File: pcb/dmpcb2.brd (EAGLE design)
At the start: 100 x 100 mm, 65 parts, among them IC1 7805DT, IC2 L293D, IC4 LM358D, IC5 LM358D, J7 SJ-3523-SMT-TR, Q1 IRF530, Q2 IRF530

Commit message: borading2..
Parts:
- added DCMOTOR1: (no value), SparkFun-Connectors:1X02_2.54_SCREWTERM
- added JP1: (no value), jumper:JP2
- added X2: (no value), con-wago-500:W237-4
- added X3: (no value), con-wago-500:W237-102
- moved IC4 247.8 mm to (16.5, 56.5), turned to 90 degrees
- moved R15 180.1 mm to (6.35, 64.1)
- moved R16 177.9 mm to (-17.8, 58.4)
- moved R10 175.2 mm to (-12.7, 47.6)
- moved JP6 163.5 mm to (19.7, 38.1)
- moved JP5 160.4 mm to (19.7, 41.3)
- moved R11 158.7 mm to (-32.4, 62.2)
- moved JP4 149.4 mm to (19.7, 44.5), turned to 180 degrees
- moved R9 145.1 mm to (-5.71, 52.1)
- moved J8 142.9 mm to (20.3, 62.2)
- moved R12 125.8 mm to (41.3, 13.3), turned to 270 degrees
- moved R13 112.5 mm to (59.7, 14.0), turned to 270 degrees
- moved JP3 110.0 mm to (8.26, 48.9)
- moved C7 48.2 mm to (13.3, 7.62), turned to 270 degrees
- moved U$2 10.8 mm to (19.7, 24.8)
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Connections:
- new net N$11: DCMOTOR1.P1, IC2.14
- new net N$12: DCMOTOR1.P2, IC2.11
- net +5V: now also JP1.3
- net A1: now also X2.2
- net A2: now also X2.1
- net B1: now also X2.3
- net B2: now also X2.4
- net GND: now also X3.2
- net V+: now also JP1.1
- net VMOT: now also JP1.2, X3.1
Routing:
- net +5V: track 184.9 -> 350.7 mm, vias 1 -> 2
- net V+: track 89.4 -> 211.0 mm
- net DRV8825SLP: track 0.00 -> 88.9 mm
- net DRV8825STEP: track 0.00 -> 81.5 mm
- net DRV8825DIR: track 0.00 -> 76.6 mm
- net N$57: track 0.00 -> 32.3 mm
- net N$11: track 0.00 -> 25.4 mm
- net N$58: track 0.00 -> 23.3 mm
- net N$59: track 0.00 -> 22.3 mm
- net N$12: track 0.00 -> 21.9 mm
- net VMOT: track 0.00 -> 19.1 mm
- net N$5: track 0.00 -> 13.6 mm
- net B2: track 0.00 -> 9.88 mm
- net A2: track 0.00 -> 9.88 mm
- net A1: track 0.00 -> 8.80 mm
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
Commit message: routing done
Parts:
- removed DCMOTOR, DCMOTOR1, SENSOR, SWITCHLOAD, SWITCHLOAD1: (no value), SparkFun-Connectors:1X02_2.54_SCREWTERM
- removed JP8: (no value), jumper:JP1
- removed SV2: (no value), con-lstb:MA08-1
- added 14/DAC: (no value), jumper:JP1
- added J3: (no value), SparkFun-Connectors:1X08
- added J4: (no value), SparkFun-Connectors:1X03_LOCK_LONGPADS
- added X4, X5, X6, X7, X8: (no value), con-wago-500:W237-102
- moved R11 47.7 mm to (15.2, 59.7)
- moved R16 40.0 mm to (21.6, 65.4), turned to 90 degrees
- moved R10 28.8 mm to (15.2, 54.6)
- moved R9 21.6 mm to (15.2, 57.1)
- moved JP3 15.7 mm to (21.6, 57.1), turned to 270 degrees
- moved X1 10.9 mm to (93.3, 85.7), flipped to the bottom, turned to 270 degrees
- moved C3 10.9 mm to (95.2, 74.9), turned to 180 degrees
- moved JP6 9.88 mm to (12.7, 45.1), turned to 90 degrees
- moved R13 9.67 mm to (63.5, 5.08)
- moved R12 9.38 mm to (36.8, 5.08)
- moved IC4 7.73 mm to (15.2, 64.1)
- moved J8 7.62 mm to (20.3, 69.8)
- moved 3.3V 7.62 mm to (82.5, 66.0)
- moved 5V 7.62 mm to (88.3, 66.0)
- moved GND 7.62 mm to (94.0, 66.0)
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- renumbered JP7 to EXT_5V
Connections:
- removed net LM293EN: IC2.1, SV2.3
- removed net LM293IN01: IC2.2, SV2.4
- removed net LM293IN02: IC2.7, SV2.5
- new net H-BRDIGE_A_02: IC2.7, J3.5
- new net H-BRIDGE_A_01: IC2.2, J3.4
- new net H-BRIDGE_A_EN: IC2.1, J3.3
- new net H-BRIDGE_B_01: IC2.15, J4.3
- new net H-BRIDGE_B_02: IC2.10, J4.2
- new net H-BRIDGE_B_EN: IC2.9, J4.1
- net +5V: now also X8.1; no longer SENSOR.P2
- net BETTERAUDIOOUT: now also 14/DAC.2; no longer JP8.2
- net BUTTON01: now also J3.1; no longer SV2.1
- net BUTTON02: now also J3.2; no longer SV2.2
- net DRV8825DIR: now also J1.1; no longer J1.2
- net DRV8825EN: now also J1.5; no longer J1.1
- net DRV8825SLP: now also J1.3; no longer J1.5
- net DRV8825STEP: now also J1.2; no longer J1.3
- net M1: now also X4.2; no longer SWITCHLOAD.P1
- net M2: now also X5.2; no longer SWITCHLOAD1.P1
- net MAX7219CLK: now also J3.7; no longer SV2.7
- net MAX7219CS: now also J3.8; no longer SV2.8
- net MAX7219DIN: now also J3.6; no longer SV2.6
- net N$11: now also X6.2; no longer DCMOTOR1.P1
- net N$12: now also X6.1; no longer DCMOTOR1.P2
- net N$5: now also X7.1; no longer DCMOTOR.P2
- net N$55: now also 14/DAC.1; no longer JP8.1
- net N$6: now also X7.2; no longer DCMOTOR.P1
- net SENSORPORT: now also X8.2; no longer SENSOR.P1
- net V+: now also X4.1, X5.1; no longer SWITCHLOAD.P2, SWITCHLOAD1.P2
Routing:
- net 3.3V: track 45.8 -> 223.8 mm, vias 0 -> 2
- net BUTTON02: track 0.00 -> 126.0 mm, vias 0 -> 3
- net POT01: track 0.00 -> 126.0 mm, vias 0 -> 3
- net H-BRIDGE_A_EN: track 0.00 -> 122.4 mm, vias 0 -> 3
- net H-BRIDGE_A_01: track 0.00 -> 116.8 mm, vias 0 -> 3
- net OPAMPOUT: track 0.00 -> 113.9 mm, vias 0 -> 2
- net BUTTON01: track 0.00 -> 111.0 mm, vias 0 -> 3
- net SENSORPORT: track 0.00 -> 108.8 mm, vias 0 -> 1
- net DRV8825EN: track 0.00 -> 102.4 mm
- net H-BRDIGE_A_02: track 0.00 -> 97.5 mm, vias 0 -> 3
- net DRV8825RST: track 0.00 -> 88.5 mm
- net POT02: track 0.00 -> 78.2 mm, vias 0 -> 2
- net N$63: track 0.00 -> 39.0 mm
- net GND: track 34.7 -> 53.4 mm, vias 5 -> 7
- net N$75: track 0.00 -> 12.1 mm, vias 0 -> 1
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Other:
- board text added: "00"
- board text added: "01"
- board text added: "02"
- board text added: "03"
- board text added: "14/DAC"
- board text added: "AUDIO_OUT"
- board text added: "BLINK. SENSE. MOVE."
- board text added: "BUT1"
- board text added: "BUT2"
- board text added: "GND"
- board text added: "digital media bremen hfk bremen v.01"

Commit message: started to add part references and values, also started adding pin names and similar. tried adding nice graphics as bmp but failed horribly...
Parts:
- R4: value 220 -> 220R
- moved J4 3.17 mm to (75.6, 27.9)
- moved R3 2.01 mm to (87.6, 80.0), turned to 90 degrees
- moved IC2 1.91 mm to (83.2, 22.9)
- moved C3 1.27 mm to (95.2, 76.2)
- moved J1 0.64 mm to (69.2, 61.6)
- moved D3 0.63 mm to (88.3, 40.6)
- moved Q2 0.63 mm to (86.4, 40.6)
- moved R1 0.63 mm to (79.4, 38.1)
- moved R2 0.63 mm to (79.4, 43.2)
- moved X4 0.63 mm to (93.3, 40.6)
- moved 3.3V 0.63 mm to (82.5, 66.7)
- moved 5V 0.63 mm to (88.3, 66.7)
- moved GND 0.63 mm to (94.0, 66.7)
- moved J2 0.63 mm to (66.7, 94.6)
- renumbered JP6 to STP_CONF, LED1 to LED_01, U$1 to TEENSY3.2, U$2 to DRV8825
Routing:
- net H-BRDIGE_A_02: track 97.5 -> 107.3 mm
- net +5V: track 354.1 -> 359.2 mm
- net BETTERAUDIOOUT: track 86.1 -> 82.6 mm
- net BUTTON02: track 126.0 -> 123.1 mm
- net H-BRIDGE_A_EN: track 122.4 -> 125.2 mm
- net POT01: track 126.0 -> 128.7 mm
- net N$8: track 6.06 -> 8.41 mm
- net N$69: track 7.87 -> 9.73 mm
- net H-BRIDGE_A_01: track 116.8 -> 118.3 mm
- net BUTTON01: track 111.0 -> 109.5 mm
- net H-BRIDGE_B_02: track 8.03 -> 6.62 mm
- net 3.3V: track 223.8 -> 224.9 mm
- net V+: track 221.8 -> 220.8 mm
- net GND: track 53.4 -> 54.2 mm
- net OPAMPOUT: track 113.9 -> 113.1 mm
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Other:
- board text added: "03 ~"
- board text added: "04 ~"
- board text added: "05 ~"
- board text added: "06 ~"
- board text added: "07"
- board text added: "08"
- board text added: "09 ~"
- board text added: "10 ~"
- board text added: "11"
- board text added: "12"
- board text added: "13/LED"
- board text added: "14/A0"
- board text added: "15/A1"
- board text added: "16/A2"
- board text added: "17/A3"
- board text added: "18/A4"
- board text added: "19/A5"
- board text added: "20/A6"
- board text added: "21/A7"
- board text added: "22/A8"
- board text added: "23/A9"
- board text added: "3.3V"
- board text added: "A14/DAC"
- board text added: "AGND"
- board text added: "B10K"
- board text added: "BUT 01"
- board text added: "BUT 02"
- board text added: "D3"
- board text added: "D4"
- board text added: "DIS CLK"
- board text added: "DIS CS"
- board text added: "DIS DIN"
- board text added: "H-Bridge"
- board text added: "HB 02"
- board text added: "HB EN"
- board text added: "HB IN 01"
- board text added: "HB IN 02"
- board text added: "IC2"
- board text added: "MCU1"
- board text added: "MOSFET 01"
- board text added: "MOSFET 02"
- board text added: "MOSFET01"
- board text added: "MOSFET02"
- board text added: "OPAMP OUT"
- board text added: "POT 01"
- board text added: "POT 02"
- board text added: "Q1"
- board text added: "Q2"
- board text added: "SENSORPORT"
- board text added: "STP CONF"
- board text added: "STP DIR"
- board text added: "STP EN"
- board text added: "STP HIGH"
- board text added: "STP LOW"
- board text added: "STP RST"
- board text added: "STP SLP"
- board text added: "STP STP"
- board text added: "TEENSY 3.2"
- board text added: "VIN"
- board text added: "~"
- board text removed: "03"
- board text removed: "14/DAC"
- board text removed: "BUT1"
- board text removed: "BUT2"

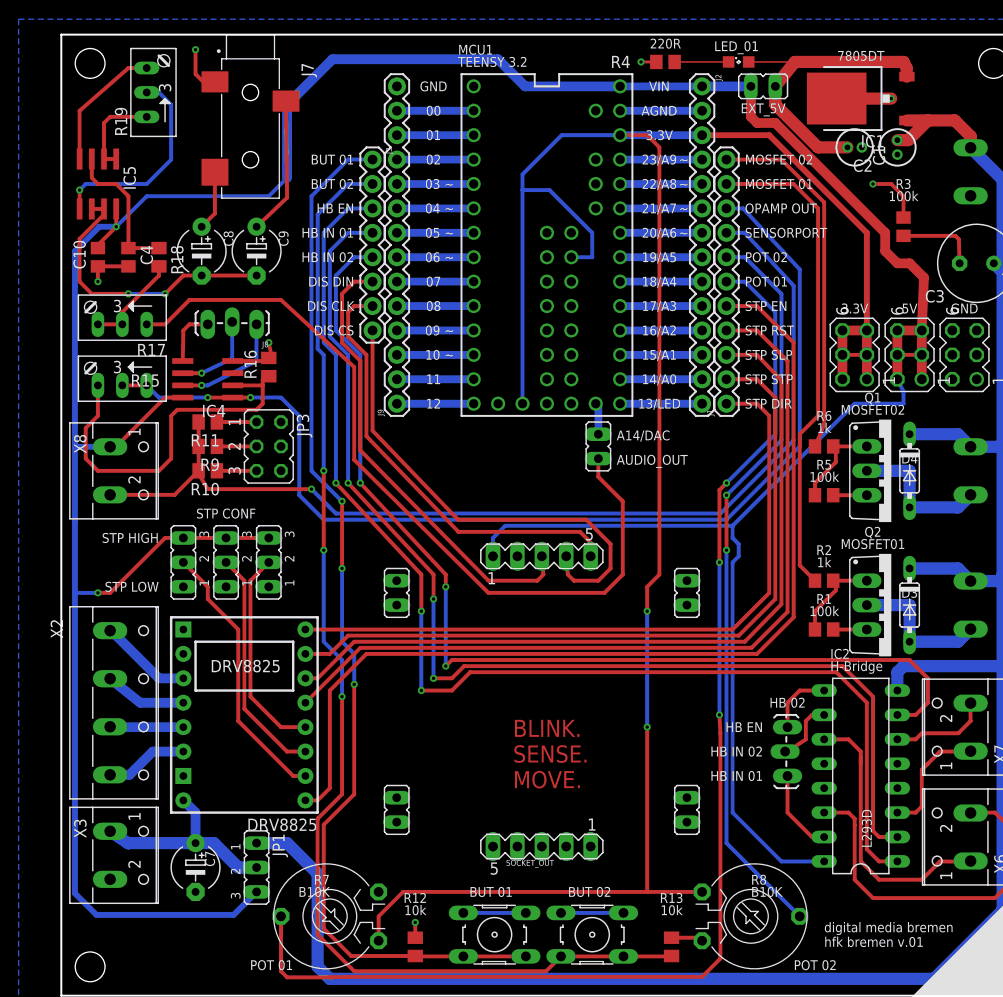
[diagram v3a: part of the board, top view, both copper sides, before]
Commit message: added component names, deleted component values. still need to add names to AKLs. Maybe drawing zones on the board would be good?
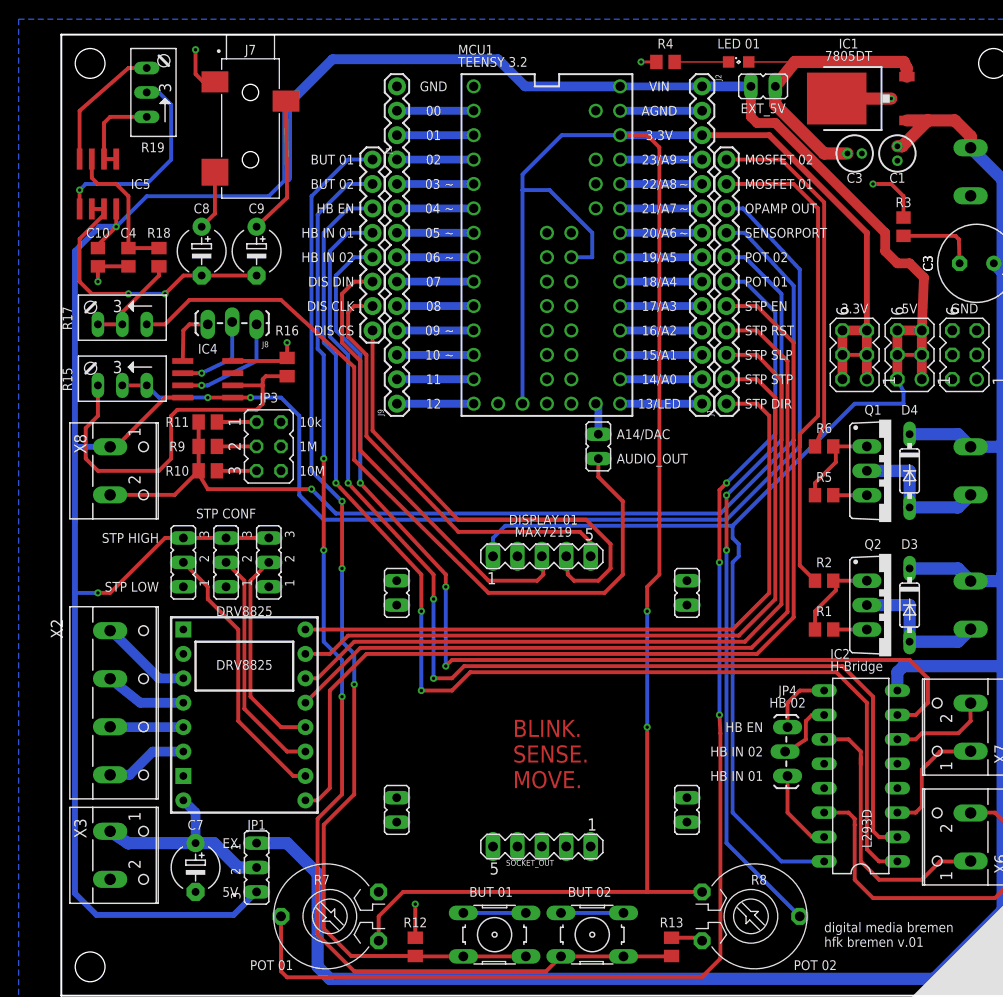
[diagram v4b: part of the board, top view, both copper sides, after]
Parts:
- moved R16 1.91 mm to (23.5, 65.4)
- moved C1 0.64 mm to (87.0, 87.6)
- moved C2 0.64 mm to (82.5, 87.6)
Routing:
- net GND: track 54.2 -> 57.7 mm
- net N$63: track 39.0 -> 40.9 mm
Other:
- board text added: "10M"
- board text added: "10k"
- board text added: "1M"
- board text added: "5V"
- board text added: "C1"
- board text added: "C10"
- board text added: "C3"
- board text added: "C4"
- board text added: "C7"
- board text added: "C8"
- board text added: "C9"
- board text added: "DISPLAY 01"
- board text added: "DRV8825"
- board text added: "EX"
- board text added: "IC1"
- board text added: "IC4"
- board text added: "IC5"
- board text added: "J7"
- board text added: "JP1"
- board text added: "JP3"
- board text added: "JP4"
- board text added: "LED 01"
- board text added: "MAX7219"
- board text added: "R1"
- board text added: "R10"
- board text added: "R11"
- board text added: "R15"
- board text added: "R16"
- board text added: "R17"
- board text added: "R18"
- board text added: "R19"
- board text added: "R2"
- board text added: "R3"
- board text added: "R4"
- board text added: "R9"
- board text removed: "B10K"
- board text removed: "MOSFET01"
- board text removed: "MOSFET02"
